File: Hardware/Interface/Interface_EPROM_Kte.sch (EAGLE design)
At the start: 24 parts, among them IC1 MCP23017SP, IC2 MCP23017SP, X1 PN61729-S

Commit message: MDIS hinzugefügt
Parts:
- added R13: (no value), resistor:R-EU_R0805
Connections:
- net 5V_KTE renamed VCCIO
- new net !MDIS: R13.1
- net +5V: now also R13.2
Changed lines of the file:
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@@
 <part name="P+11" library="supply1" deviceset="+5V" device=""/>
 <part name="FRAME1" library="frames" deviceset="DINA4_L" device=""/>
+<part name="VCC1" library="supply1" deviceset="VCCIO" device=""/>
+<part name="R13" library="resistor" deviceset="R-EU_" device="R0805"/>
+<part name="P+12" library="supply1" deviceset="+5V" device=""/>
 </parts>
 <sheets>
@@
 <instance part="FRAME1" gate="G$1" x="0" y="0"/>
 <instance part="FRAME1" gate="G$2" x="162.56" y="0"/>
+<instance part="VCC1" gate="G$1" x="200.66" y="172.72"/>
+<instance part="R13" gate="G$1" x="149.86" y="88.9" rot="R180"/>
+<instance part="P+12" gate="1" x="142.24" y="93.98"/>
 </instances>
 <busses>
@@
 <wire x1="109.22" y1="68.58" x2="109.22" y2="73.66" width="0.1524" layer="91"/>
 </segment>
+<segment>
+<pinref part="R13" gate="G$1" pin="2"/>
+<pinref part="P+12" gate="1" pin="+5V"/>
+<wire x1="144.78" y1="88.9" x2="142.24" y2="88.9" width="0.1524" layer="91"/>
+<wire x1="142.24" y1="88.9" x2="142.24" y2="91.44" width="0.1524" layer="91"/>
+</segment>
 </net>
 <net name="N$7" class="0">
@@
 </segment>
 </net>
-<net name="5V_KTE" class="0">
+<net name="VUSB" class="0">
+<segment>
+<pinref part="U$2" gate="IC$1" pin="VUSB"/>
+<pinref part="C5" gate="G$1" pin="2"/>
+<wire x1="25.4" y1="88.9" x2="20.32" y2="88.9" width="0.1524" layer="91"/>
+<wire x1="20.32" y1="88.9" x2="20.32" y2="83.82" width="0.1524" layer="91"/>
+</segment>
+</net>
+<net name="N$8" class="0">
+<segment>
+<pinref part="LED1" gate="G$1" pin="A"/>
+<pinref part="R10" gate="G$1" pin="1"/>
+</segment>
+</net>
+<net name="USB_D-" class="0">
+<segment>
+<pinref part="X1" gate="G$1" pin="2"/>
+<wire x1="15.24" y1="101.6" x2="17.78" y2="101.6" width="0.1524" layer="91"/>
+<wire x1="17.78" y1="101.6" x2="20.32" y2="99.06" width="0.1524" layer="91"/>
+<pinref part="U$2" gate="IC$1" pin="D-"/>
+<wire x1="20.32" y1="99.06" x2="25.4" y2="99.06" width="0.1524" layer="91"/>
+</segment>
+</net>
+<net name="USB_D+" class="0">
+<segment>
+<pinref part="X1" gate="G$1" pin="3"/>
+<wire x1="15.24" y1="99.06" x2="17.78" y2="99.06" width="0.1524" layer="91"/>
+<wire x1="17.78" y1="99.06" x2="20.32" y2="101.6" width="0.1524" layer="91"/>
+<pinref part="U$2" gate="IC$1" pin="D+"/>
+<wire x1="20.32" y1="101.6" x2="25.4" y2="101.6" width="0.1524" layer="91"/>
+</segment>
+</net>
+<net name="I2C_ACT" class="0">
+<segment>
+<pinref part="U$2" gate="IC$1" pin="GP3"/>
+<pinref part="LED1" gate="G$1" pin="C"/>
+<wire x1="55.88" y1="93.98" x2="58.42" y2="93.98" width="0.1524" layer="91"/>
+</segment>
+</net>
+<net name="PWR_EXT_ON" class="0">
+<segment>
+<pinref part="U$1" gate="ST890C" pin="!ON"/>
+<wire x1="172.72" y1="160.02" x2="175.26" y2="160.02" width="0.1524" layer="91"/>
+<wire x1="175.26" y1="160.02" x2="175.26" y2="99.06" width="0.1524" layer="91"/>
+<wire x1="175.26" y1="99.06" x2="134.62" y2="99.06" width="0.1524" layer="91"/>
+<pinref part="IC1" gate="G$1" pin="GPB4"/>
+</segment>
+</net>
+<net name="PWR_EXT_FAULT" class="0">
+<segment>
+<pinref part="U$1" gate="ST890C" pin="!FAULT"/>
+<wire x1="144.78" y1="160.02" x2="137.16" y2="160.02" width="0.1524" layer="91"/>
+<wire x1="137.16" y1="160.02" x2="137.16" y2="96.52" width="0.1524" layer="91"/>
+<pinref part="IC1" gate="G$1" pin="GPB5"/>
+<wire x1="137.16" y1="96.52" x2="134.62" y2="96.52" width="0.1524" layer="91"/>
+</segment>
+</net>
+<net name="N$11" class="0">
+<segment>
+<pinref part="LD1" gate="G$1" pin="AG"/>
+<pinref part="R11" gate="G$1" pin="2"/>
+</segment>
+</net>
+<net name="N$12" class="0">
+<segment>
+<pinref part="LD1" gate="G$1" pin="AR"/>
+<pinref part="R12" gate="G$1" pin="1"/>
+</segment>
+</net>
+<net name="!RD" class="0">
+<segment>
+<pinref part="IC1" gate="G$1" pin="GPB0"/>
+<wire x1="139.7" y1="109.22" x2="134.62" y2="109.22" width="0.1524" layer="91"/>
+<label x="142.24" y="109.22" size="1.778" layer="95"/>
+</segment>
+</net>
+<net name="!WR" class="0">
+<segment>
+<pinref part="IC1" gate="G$1" pin="GPB1"/>
+<wire x1="139.7" y1="106.68" x2="134.62" y2="106.68" width="0.1524" layer="91"/>
+<label x="142.24" y="106.68" size="1.778" layer="95"/>
+</segment>
+</net>
+<net name="!IOREQ" class="0">
+<segment>
+<pinref part="IC1" gate="G$1" pin="GPB3"/>
+<wire x1="139.7" y1="101.6" x2="134.62" y2="101.6" width="0.1524" layer="91"/>
+<label x="142.24" y="101.6" size="1.778" layer="95"/>
+</segment>
+</net>
+<net name="!MREQ" class="0">
+<segment>
+<pinref part="IC1" gate="G$1" pin="GPB2"/>
+<wire x1="139.7" y1="104.14" x2="134.62" y2="104.14" width="0.1524" layer="91"/>
+<label x="142.24" y="104.14" size="1.778" layer="95"/>
+</segment>
+</net>
+<net name="VCCIO" class="0">
 <segment>
 <pinref part="U$1" gate="ST890C" pin="OUT1"/>
@@
 <wire x1="182.88" y1="167.64" x2="190.5" y2="167.64" width="0.1524" layer="91"/>
 <pinref part="R12" gate="G$1" pin="2"/>
-</segment>
-</net>
-<net name="VUSB" class="0">
-<segment>
-<pinref part="U$2" gate="IC$1" pin="VUSB"/>
-<pinref part="C5" gate="G$1" pin="2"/>
-<wire x1="25.4" y1="88.9" x2="20.32" y2="88.9" width="0.1524" layer="91"/>
-<wire x1="20.32" y1="88.9" x2="20.32" y2="83.82" width="0.1524" layer="91"/>
-</segment>
-</net>
-<net name="N$8" class="0">
-<segment>
-<pinref part="LED1" gate="G$1" pin="A"/>
-<pinref part="R10" gate="G$1" pin="1"/>
-</segment>
-</net>
-<net name="USB_D-" class="0">
-<segment>
-<pinref part="X1" gate="G$1" pin="2"/>
-<wire x1="15.24" y1="101.6" x2="17.78" y2="101.6" width="0.1524" layer="91"/>
-<wire x1="17.78" y1="101.6" x2="20.32" y2="99.06" width="0.1524" layer="91"/>
-<pinref part="U$2" gate="IC$1" pin="D-"/>
-<wire x1="20.32" y1="99.06" x2="25.4" y2="99.06" width="0.1524" layer="91"/>
-</segment>
-</net>
-<net name="USB_D+" class="0">
-<segment>
-<pinref part="X1" gate="G$1" pin="3"/>
-<wire x1="15.24" y1="99.06" x2="17.78" y2="99.06" width="0.1524" layer="91"/>
-<wire x1="17.78" y1="99.06" x2="20.32" y2="101.6" width="0.1524" layer="91"/>
-<pinref part="U$2" gate="IC$1" pin="D+"/>
-<wire x1="20.32" y1="101.6" x2="25.4" y2="101.6" width="0.1524" layer="91"/>
-</segment>
-</net>
-<net name="I2C_ACT" class="0">
-<segment>
-<pinref part="U$2" gate="IC$1" pin="GP3"/>
-<pinref part="LED1" gate="G$1" pin="C"/>
-<wire x1="55.88" y1="93.98" x2="58.42" y2="93.98" width="0.1524" layer="91"/>
-</segment>
-</net>
-<net name="PWR_EXT_ON" class="0">
-<segment>
-<pinref part="U$1" gate="ST890C" pin="!ON"/>
-<wire x1="172.72" y1="160.02" x2="175.26" y2="160.02" width="0.1524" layer="91"/>
-<wire x1="175.26" y1="160.02" x2="175.26" y2="99.06" width="0.1524" layer="91"/>
-<wire x1="175.26" y1="99.06" x2="134.62" y2="99.06" width="0.1524" layer="91"/>
-<pinref part="IC1" gate="G$1" pin="GPB4"/>
-</segment>
-</net>
-<net name="PWR_EXT_FAULT" class="0">
-<segment>
-<pinref part="U$1" gate="ST890C" pin="!FAULT"/>
-<wire x1="144.78" y1="160.02" x2="137.16" y2="160.02" width="0.1524" layer="91"/>
-<wire x1="137.16" y1="160.02" x2="137.16" y2="96.52" width="0.1524" layer="91"/>
-<pinref part="IC1" gate="G$1" pin="GPB5"/>
-<wire x1="137.16" y1="96.52" x2="134.62" y2="96.52" width="0.1524" layer="91"/>
-</segment>
-</net>
-<net name="N$11" class="0">
-<segment>
-<pinref part="LD1" gate="G$1" pin="AG"/>
-<pinref part="R11" gate="G$1" pin="2"/>
-</segment>
-</net>
-<net name="N$12" class="0">
-<segment>
-<pinref part="LD1" gate="G$1" pin="AR"/>
-<pinref part="R12" gate="G$1" pin="1"/>
-</segment>
-</net>
-<net name="!RD" class="0">
-<segment>
-<pinref part="IC1" gate="G$1" pin="GPB0"/>
-<wire x1="139.7" y1="109.22" x2="134.62" y2="109.22" width="0.1524" layer="91"/>
-<label x="142.24" y="109.22" size="1.778" layer="95"/>
-</segment>
-</net>
-<net name="!WR" class="0">
-<segment>
-<pinref part="IC1" gate="G$1" pin="GPB1"/>
-<wire x1="139.7" y1="106.68" x2="134.62" y2="106.68" width="0.1524" layer="91"/>
-<label x="142.24" y="106.68" size="1.778" layer="95"/>
-</segment>
-</net>
-<net name="!IOREQ" class="0">
-<segment>
-<pinref part="IC1" gate="G$1" pin="GPB3"/>
-<wire x1="139.7" y1="101.6" x2="134.62" y2="101.6" width="0.1524" layer="91"/>
-<label x="142.24" y="101.6" size="1.778" layer="95"/>
-</segment>
-</net>
-<net name="!MREQ" class="0">
-<segment>
-<pinref part="IC1" gate="G$1" pin="GPB2"/>
-<wire x1="139.7" y1="104.14" x2="134.62" y2="104.14" width="0.1524" layer="91"/>
-<label x="142.24" y="104.14" size="1.778" layer="95"/>
-</segment>
-</net>
+<wire x1="190.5" y1="167.64" x2="200.66" y2="167.64" width="0.1524" layer="91"/>
+<junction x="190.5" y="167.64"/>
+<pinref part="VCC1" gate="G$1" pin="VCCIO"/>
+<wire x1="200.66" y1="167.64" x2="200.66" y2="170.18" width="0.1524" layer="91"/>
+</segment>
+</net>
+<net name="!MDIS" class="0">
+<segment>
+<pinref part="R13" gate="G$1" pin="1"/>
+<wire x1="154.94" y1="88.9" x2="167.64" y2="88.9" width="0.1524" layer="91"/>
+<label x="160.02" y="86.36" size="1.778" layer="95"/>
+</segment>
+</net>

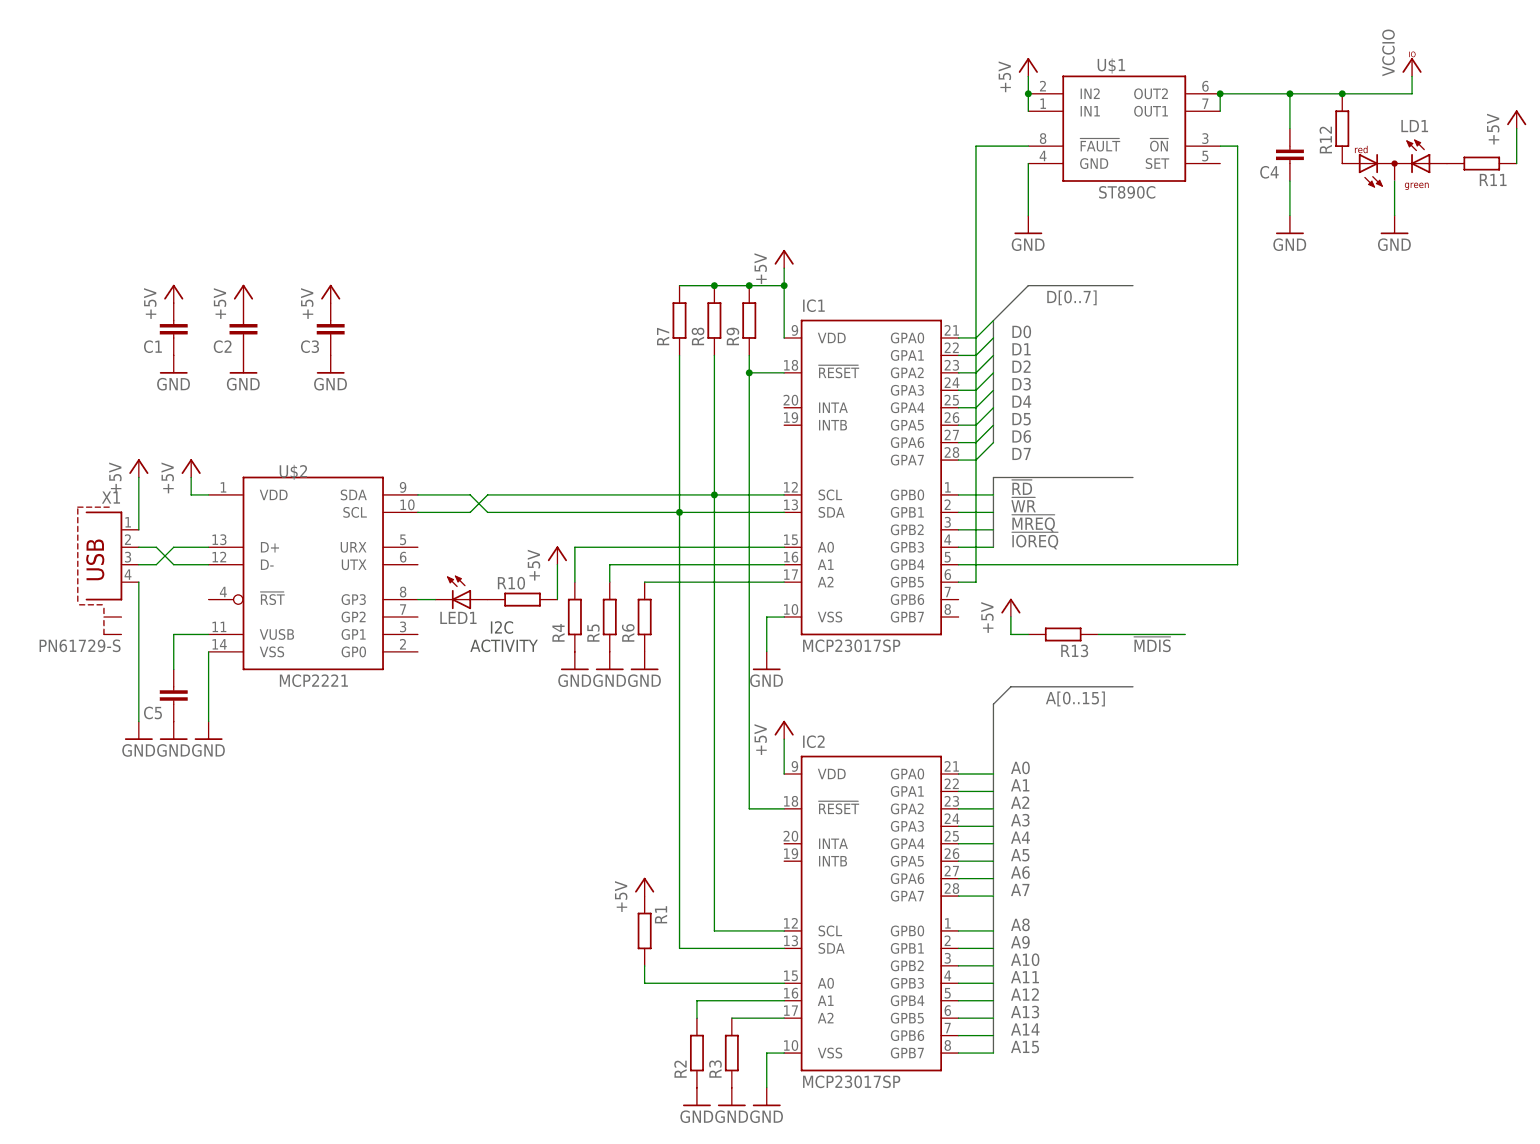
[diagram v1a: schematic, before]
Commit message: Taster für GPIO-Reset hinzugefügt, sowie externer Anschluss der 5V für Target
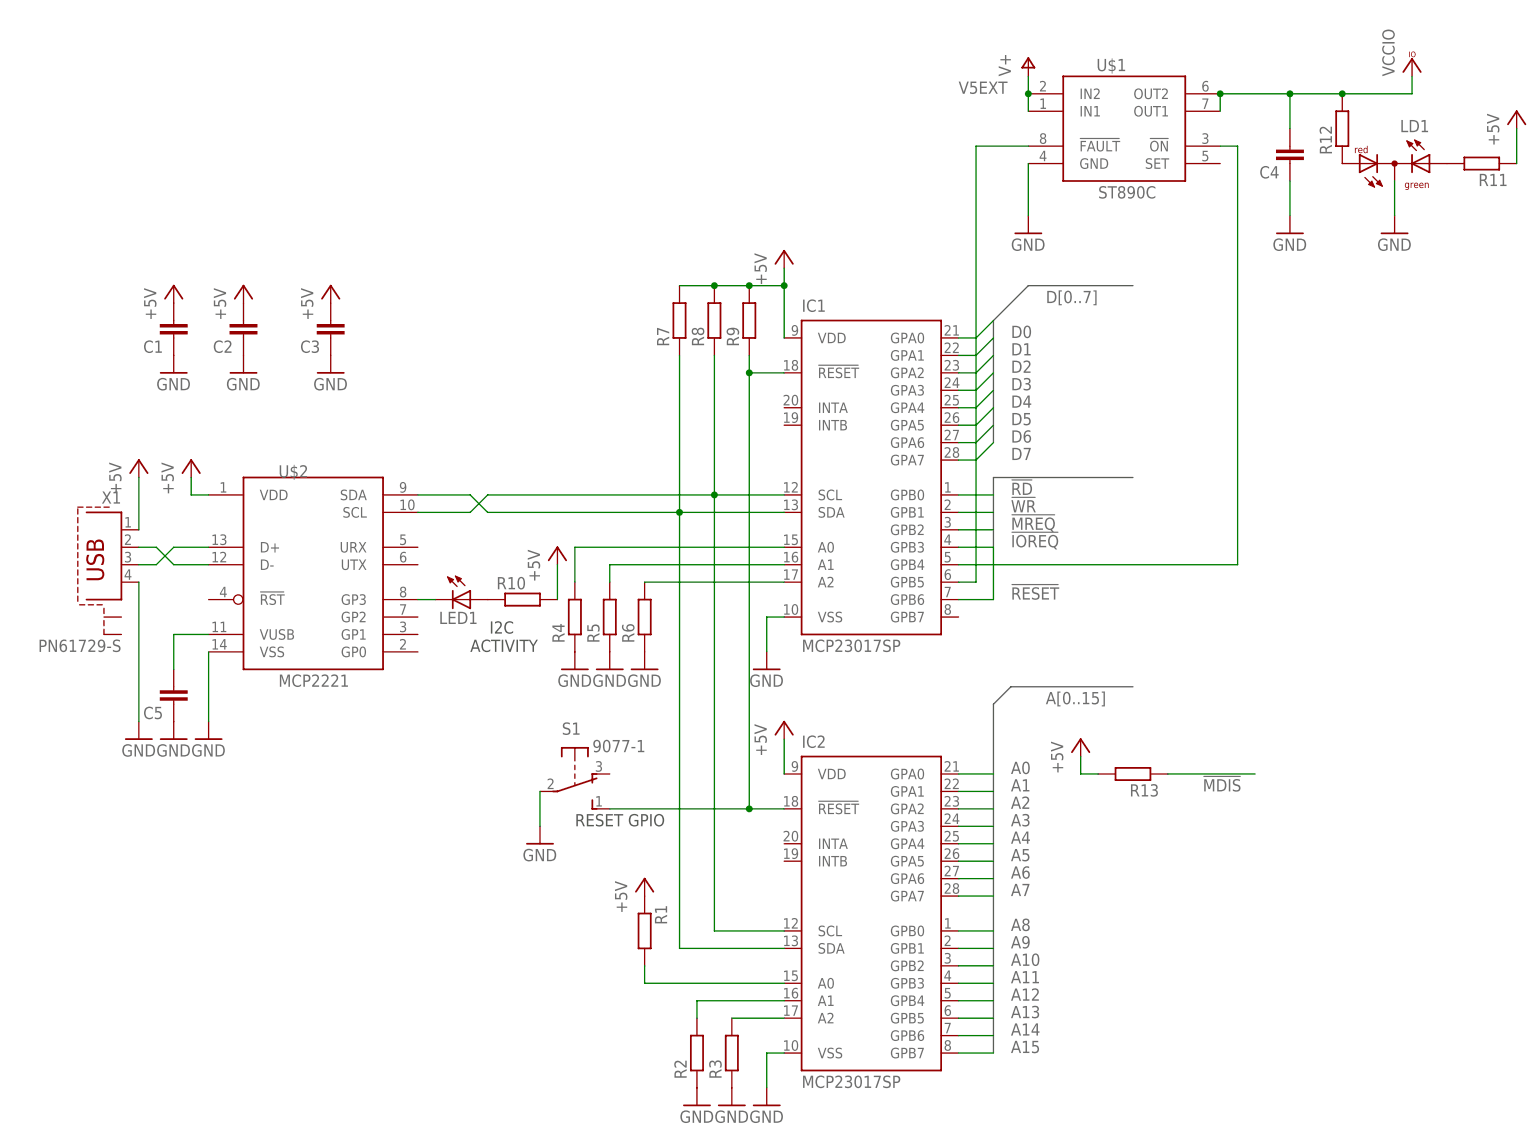
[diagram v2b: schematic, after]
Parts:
- added S1: 9077-1, switch-misc:9077-1
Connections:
- new net !RESET: IC1.GPB6
- new net V5EXT: U$1.IN1, U$1.IN2
- net +5V: no longer U$1.IN1, U$1.IN2
- net GND: now also S1.P
- net N$7: now also S1.S
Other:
- note added: "RESET GPIO"
- moved on the sheet: R13
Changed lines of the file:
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@@
 <part name="P+5" library="supply1" deviceset="+5V" device=""/>
 <part name="U$1" library="ST890" deviceset="ST890C" device=""/>
-<part name="P+6" library="supply1" deviceset="+5V" device=""/>
 <part name="GND11" library="supply1" deviceset="GND" device=""/>
 <part name="C4" library="resistor" deviceset="C-EU" device="C0805"/>
@@
 <part name="R13" library="resistor" deviceset="R-EU_" device="R0805"/>
 <part name="P+12" library="supply1" deviceset="+5V" device=""/>
+<part name="S1" library="switch-misc" deviceset="9077-1" device=""/>
+<part name="GND17" library="supply1" deviceset="GND" device=""/>
+<part name="P+6" library="supply1" deviceset="V+" device=""/>
 </parts>
 <sheets>
@@
 <text x="63.5" y="86.36" size="1.778" layer="97">    I2C
 ACTIVITY</text>
+<text x="78.74" y="60.96" size="1.778" layer="97">RESET GPIO</text>
 </plain>
 <instances>
@@
 <instance part="P+5" gate="1" x="43.18" y="139.7"/>
 <instance part="U$1" gate="ST890C" x="149.86" y="154.94"/>
-<instance part="P+6" gate="1" x="144.78" y="172.72"/>
 <instance part="GND11" gate="1" x="144.78" y="147.32"/>
 <instance part="C4" gate="G$1" x="182.88" y="157.48" rot="R180"/>
@@
 <instance part="FRAME1" gate="G$2" x="162.56" y="0"/>
 <instance part="VCC1" gate="G$1" x="200.66" y="172.72"/>
-<instance part="R13" gate="G$1" x="149.86" y="88.9" rot="R180"/>
-<instance part="P+12" gate="1" x="142.24" y="93.98"/>
+<instance part="R13" gate="G$1" x="160.02" y="68.58" rot="R180"/>
+<instance part="P+12" gate="1" x="152.4" y="73.66"/>
+<instance part="S1" gate="1" x="78.74" y="66.04" rot="R270"/>
+<instance part="GND17" gate="1" x="73.66" y="58.42"/>
+<instance part="P+6" gate="1" x="144.78" y="172.72"/>
 </instances>
 <busses>
@@
 <pinref part="GND16" gate="1" pin="GND"/>
 <wire x1="198.12" y1="154.94" x2="198.12" y2="149.86" width="0.1524" layer="91"/>
+</segment>
+<segment>
+<pinref part="S1" gate="1" pin="P"/>
+<pinref part="GND17" gate="1" pin="GND"/>
+<wire x1="73.66" y1="66.04" x2="73.66" y2="60.96" width="0.1524" layer="91"/>
 </segment>
 </net>
@@
 </segment>
 <segment>
-<pinref part="U$1" gate="ST890C" pin="IN1"/>
-<pinref part="U$1" gate="ST890C" pin="IN2"/>
-<wire x1="144.78" y1="165.1" x2="144.78" y2="167.64" width="0.1524" layer="91"/>
-<junction x="144.78" y="167.64"/>
-<pinref part="P+6" gate="1" pin="+5V"/>
-<wire x1="144.78" y1="167.64" x2="144.78" y2="170.18" width="0.1524" layer="91"/>
-</segment>
-<segment>
 <pinref part="P+7" gate="1" pin="+5V"/>
 <pinref part="U$2" gate="IC$1" pin="VDD"/>
@@
 <pinref part="R13" gate="G$1" pin="2"/>
 <pinref part="P+12" gate="1" pin="+5V"/>
-<wire x1="144.78" y1="88.9" x2="142.24" y2="88.9" width="0.1524" layer="91"/>
-<wire x1="142.24" y1="88.9" x2="142.24" y2="91.44" width="0.1524" layer="91"/>
+<wire x1="154.94" y1="68.58" x2="152.4" y2="68.58" width="0.1524" layer="91"/>
+<wire x1="152.4" y1="68.58" x2="152.4" y2="71.12" width="0.1524" layer="91"/>
 </segment>
 </net>
@@
 <wire x1="109.22" y1="127" x2="104.14" y2="127" width="0.1524" layer="91"/>
 <junction x="104.14" y="127"/>
+<pinref part="S1" gate="1" pin="S"/>
+<wire x1="104.14" y1="63.5" x2="83.82" y2="63.5" width="0.1524" layer="91"/>
+<junction x="104.14" y="63.5"/>
 </segment>
 </net>
@@
 <segment>
 <pinref part="R13" gate="G$1" pin="1"/>
-<wire x1="154.94" y1="88.9" x2="167.64" y2="88.9" width="0.1524" layer="91"/>
-<label x="160.02" y="86.36" size="1.778" layer="95"/>
-</segment>
-</net>
+<wire x1="165.1" y1="68.58" x2="177.8" y2="68.58" width="0.1524" layer="91"/>
+<label x="170.18" y="66.04" size="1.778" layer="95"/>
+</segment>
+</net>
+<net name="!RESET" class="0">
+<segment>
+<pinref part="IC1" gate="G$1" pin="GPB6"/>
+<wire x1="139.7" y1="101.6" x2="139.7" y2="93.98" width="0.1524" layer="91"/>
+<wire x1="139.7" y1="93.98" x2="134.62" y2="93.98" width="0.1524" layer="91"/>
+<label x="142.24" y="93.98" size="1.778" layer="95"/>
+</segment>
+</net>
+<net name="V5EXT" class="0">
+<segment>
+<pinref part="U$1" gate="ST890C" pin="IN1"/>
+<pinref part="U$1" gate="ST890C" pin="IN2"/>
+<wire x1="144.78" y1="165.1" x2="144.78" y2="167.64" width="0.1524" layer="91"/>
+<junction x="144.78" y="167.64"/>
+<wire x1="144.78" y1="167.64" x2="144.78" y2="170.18" width="0.1524" layer="91"/>
+<pinref part="P+6" gate="1" pin="V+"/>
+<label x="134.62" y="167.64" size="1.778" layer="95"/>
+</segment>
+</net>
